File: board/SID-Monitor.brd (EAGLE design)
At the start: 69.8 x 120.7 mm, 107 parts, among them IC1 LM317, IC2 LM337, IC3 TLE2082, IC4 TLE2082, IC5 MAX275ACP, IC6 TLE2082, IC7 TLE2082, IC8 TLE2082, IC9 PHOTON_WITH_HEADERS, J101 POWERJACK-PTH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

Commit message: Board layout first pass
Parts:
- added U$1, U$2, U$3: (no value), SaintGimp:MOUNTING-HOLE-3.2MM
- C401, C402: device SaintGimp:CAPACITOR-2.5MM -> SaintGimp:CAPACITOR-5MM
- IC9: value PHOTON_WITH_HEADERS -> PHOTON
- moved C701 73.8 mm to (65.4, 5.71), turned to 270 degrees
- moved C1001 67.1 mm to (2.54, 36.8), turned to 180 degrees
- moved C1002 62.5 mm to (17.8, 45.1), turned to 90 degrees
- moved R702 60.2 mm to (63.5, 12.1), turned to 180 degrees
- moved R701 59.9 mm to (63.5, 14.6), turned to 180 degrees
- moved R801 57.1 mm to (57.1, 5.71), turned to 270 degrees
- moved IC9 51.0 mm to (10.2, 15.9)
- moved R802 50.4 mm to (59.7, 5.71), turned to 270 degrees
- moved R806 49.3 mm to (52.1, 5.71), turned to 270 degrees
- moved C801 49.2 mm to (54.6, 5.71), turned to 270 degrees
- moved RV401 45.5 mm to (34.3, 45.1), turned to 90 degrees
- moved JP401 43.8 mm to (38.1, 53.3), turned to 180 degrees
- moved JP403 43.3 mm to (58.4, 53.3)
- moved RV402 42.2 mm to (52.1, 45.1), turned to 270 degrees
- moved R805 41.6 mm to (45.7, 14.6)
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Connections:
- new net N$39: IC8.6, IC8.7
- net GND: now also IC8.5
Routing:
- net +5V: track 86.3 -> 296.3 mm
- net -5V: track 121.6 -> 278.1 mm, vias 0 -> 4
- net N$38: track 0.00 -> 49.1 mm, vias 0 -> 3
- net N$20: track 0.00 -> 39.1 mm, vias 0 -> 1
- net N$15: track 0.00 -> 36.2 mm
- net N$55: track 0.00 -> 32.6 mm
- net N$18: track 0.00 -> 32.1 mm
- net N$59: track 0.00 -> 31.7 mm
- net N$11: track 0.00 -> 31.6 mm
- net N$35: track 0.00 -> 29.7 mm
- net N$17: track 0.00 -> 27.7 mm
- net N$28: track 0.00 -> 24.1 mm
- net N$45: track 0.00 -> 23.9 mm
- net N$58: track 0.00 -> 22.4 mm
- net N$13: track 0.00 -> 22.1 mm
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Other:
- board size 69.8 x 120.7 mm -> 69.2 x 104.1 mm

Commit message: Version 1.0.0 sent out for manufacturing
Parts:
- turned C105 to 90 degrees
- turned D102 to 270 degrees
- turned D105 to 180 degrees
- turned D106 to 180 degrees
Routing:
- net -5V: track 278.1 -> 293.2 mm
- net +5V: track 296.3 -> 303.0 mm
- net N$4: track 20.4 -> 25.5 mm
- net N$1: track 44.9 -> 42.8 mm
- net N$61: track 32.4 -> 30.8 mm
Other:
- board text added: "SaintGimp SID-Monitor v1.0.0"

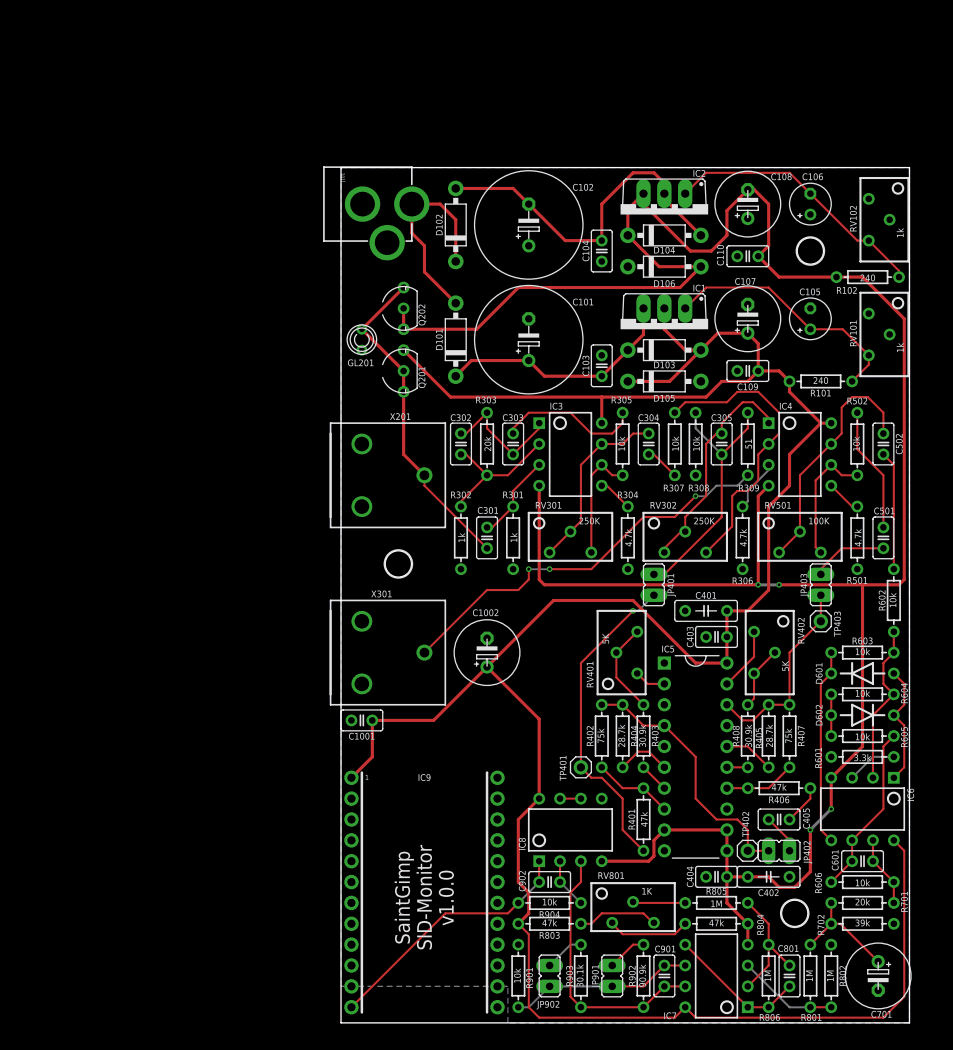
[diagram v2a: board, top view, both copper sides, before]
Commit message: Update values to tune to 25.2 kHz
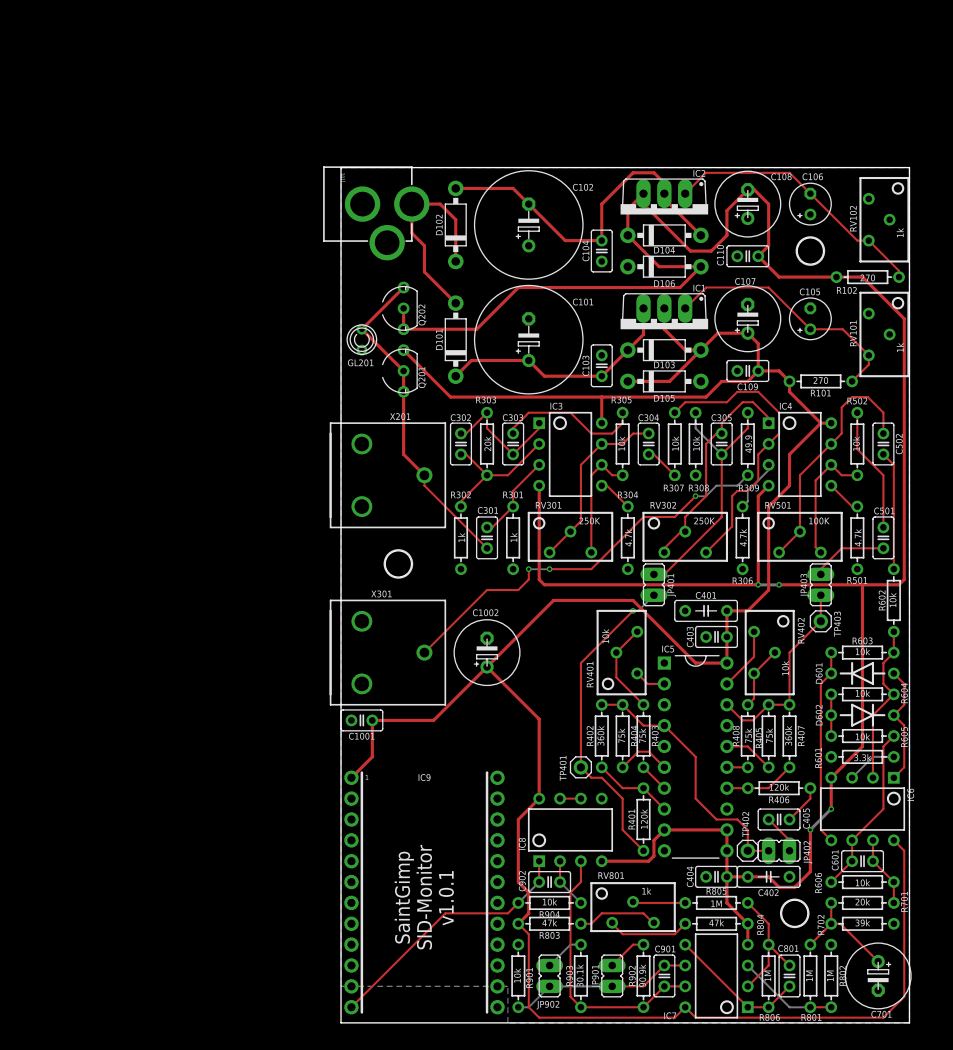
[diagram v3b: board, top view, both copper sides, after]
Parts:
- R101, R102: value 240 -> 270
- R309: value 51 -> 49.9
- R401, R406: value 47k -> 120k
- R402, R407: value 75k -> 360k
- R403, R408: value 30.9k -> 75k
- R404, R405: value 28.7k -> 75k
- RV401, RV402: value 5K -> 10k
- RV801: value 1K -> 1k
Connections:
- net GND: now also RV102.1
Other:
- board text added: "SaintGimp SID-Monitor v1.0.1"
- board text removed: "SaintGimp SID-Monitor v1.0.0"
